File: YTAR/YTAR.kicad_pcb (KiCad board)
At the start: 2 copper layers, 37 parts, among them J1 STDC14, SW1 Tact, U1 STM32H750XBHx, Y1 25MHz

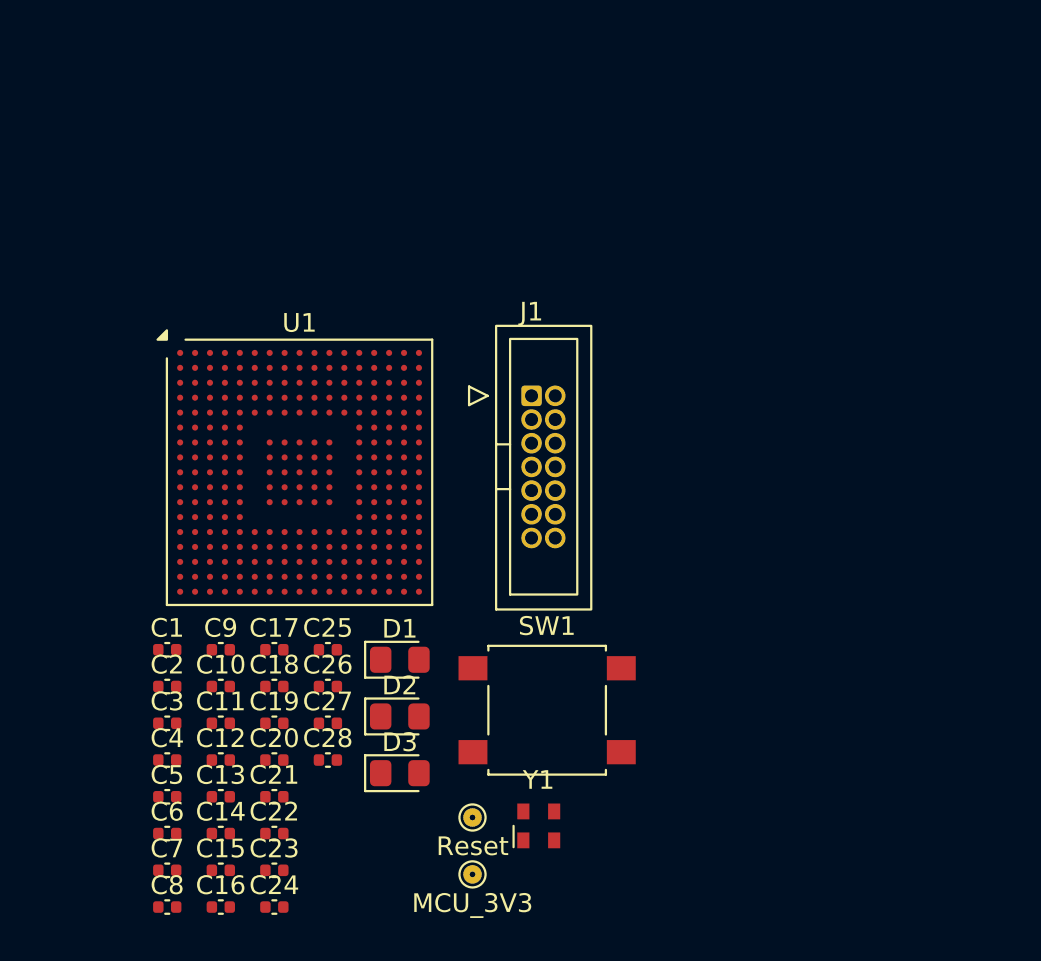
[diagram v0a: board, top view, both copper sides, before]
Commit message: DRAM added
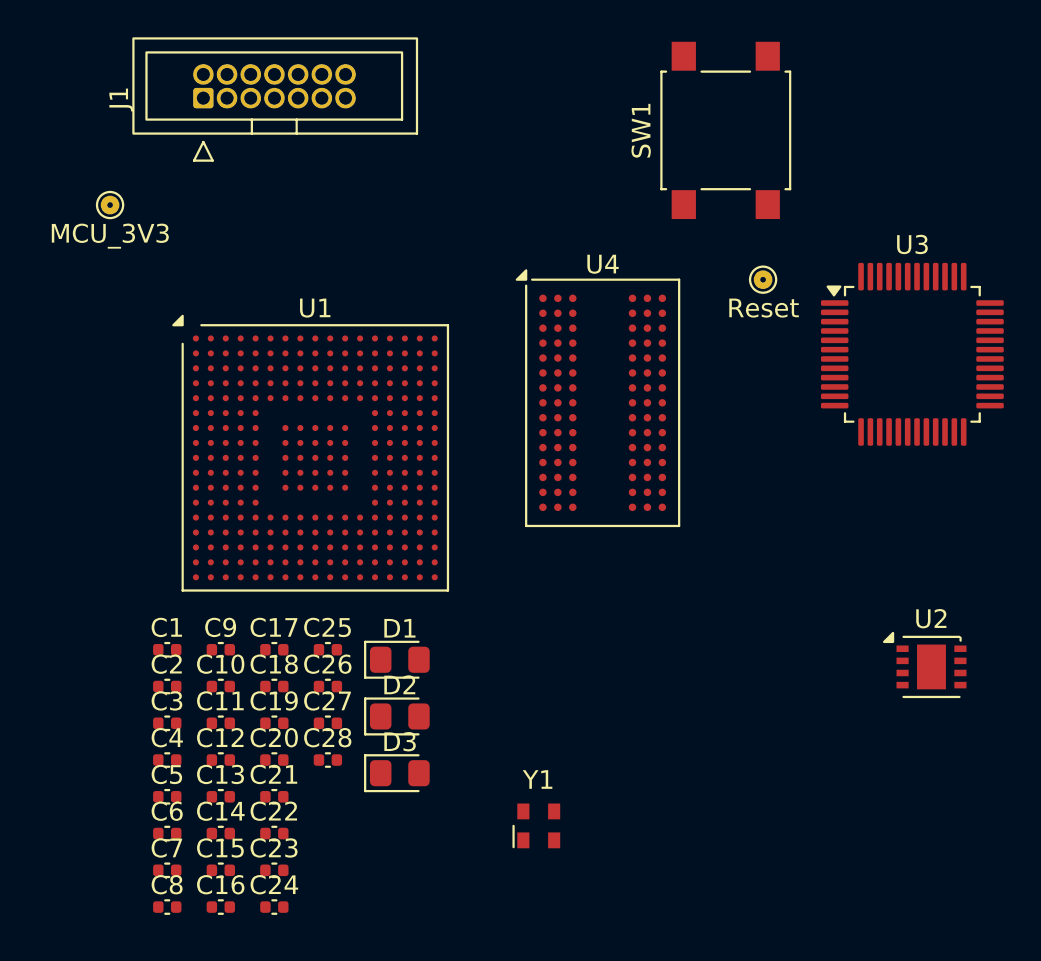
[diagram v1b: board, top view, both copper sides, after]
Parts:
- added U2: MCP2562-E-MF, Package_DFN_QFN:DFN-8-1EP_3x3mm_P0.65mm_EP1.55x2.4mm, F.Cu at (75.0, 48.8)
- added U3: DS90C124, Package_QFP:TQFP-48_7x7mm_P0.5mm, F.Cu at (74.0, 32.0)
- added U4: ~, Package_BGA:BGA-90_8.0x13.0mm_Layout2x3x15_P0.8mm, F.Cu at (57.4, 34.6)
- moved TP2 40.8 mm to (31.0, 24.0)
- moved TP1 32.8 mm to (66.0, 28.0)
- moved SW1 32.5 mm to (64.0, 20.0), turned to 90 degrees
- moved J1 23.7 mm to (36.0, 18.3), turned to 90 degrees
- moved U1 1.15 mm to (42.0, 37.5)

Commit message: Podłączono kwarc
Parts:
- added C29: 100n, Capacitor_SMD:C_0402_1005Metric, F.Cu at (35.1, 92.0)
- added C30: 100n, Capacitor_SMD:C_0402_1005Metric, F.Cu at (35.1, 94.0)
- added C31: 100n, Capacitor_SMD:C_0402_1005Metric, F.Cu at (35.1, 96.0)
- added C32: 100n, Capacitor_SMD:C_0402_1005Metric, F.Cu at (35.1, 98.0)
- added C33: 100n, Capacitor_SMD:C_0402_1005Metric, F.Cu at (35.1, 99.9)
- added C34: 100n, Capacitor_SMD:C_0402_1005Metric, F.Cu at (35.1, 101.9)
- added C35: 100n, Capacitor_SMD:C_0402_1005Metric, F.Cu at (35.1, 103.9)
- added C36: 100n, Capacitor_SMD:C_0402_1005Metric, F.Cu at (38.0, 92.0)
- added C37: 100n, Capacitor_SMD:C_0402_1005Metric, F.Cu at (38.0, 94.0)
- added C38: 100n, Capacitor_SMD:C_0402_1005Metric, F.Cu at (38.0, 96.0)
- added C39: 100n, Capacitor_SMD:C_0402_1005Metric, F.Cu at (38.0, 98.0)
- added C40: 100n, Capacitor_SMD:C_0402_1005Metric, F.Cu at (38.0, 99.9)
- added C41: 100n, Capacitor_SMD:C_0402_1005Metric, F.Cu at (38.0, 101.9)
- added C42: 100n, Capacitor_SMD:C_0402_1005Metric, F.Cu at (38.0, 103.9)
- added C43: 100n, Capacitor_SMD:C_0402_1005Metric, F.Cu at (40.8, 92.0)
- added C44: 100n, Capacitor_SMD:C_0402_1005Metric, F.Cu at (40.8, 94.0)
- added C45: 100n, Capacitor_SMD:C_0402_1005Metric, F.Cu at (40.8, 96.0)
- added C46: 100n, Capacitor_SMD:C_0402_1005Metric, F.Cu at (40.8, 98.0)
- added C47: 100n, Capacitor_SMD:C_0402_1005Metric, F.Cu at (40.8, 99.9)
- added C48: 100n, Capacitor_SMD:C_0402_1005Metric, F.Cu at (40.8, 101.9)
- added C49: 100n, Capacitor_SMD:C_0402_1005Metric, F.Cu at (40.8, 103.9)
- added C50: 100n, Capacitor_SMD:C_0402_1005Metric, F.Cu at (43.7, 92.0)
- added C51: 100n, Capacitor_SMD:C_0402_1005Metric, F.Cu at (43.7, 94.0)
- added C52: 100n, Capacitor_SMD:C_0402_1005Metric, F.Cu at (43.7, 96.0)
- added C53: 100n, Capacitor_SMD:C_0402_1005Metric, F.Cu at (43.7, 98.0)
- added J2: Conn_2x04_2.54mm_male_vertical, Connector_PinSocket_2.54mm:PinSocket_2x04_P2.54mm_Vertical, F.Cu at (50.0, 93.4)
- added J3: USB_C_Receptacle_USB2.0_NO_SBU, Connector_USB:USB_C_Receptacle_GCT_USB4085, F.Cu at (21.4, 29.0)
- added JP1: ~, MEMS_Passive:R_0805_2012Metric_Jumper_Open, F.Cu at (56.2, 74.6)
- added JP2: ~, MEMS_Passive:R_0805_2012Metric_Jumper_Open, F.Cu at (56.2, 77.6)
- added JP3: ~, MEMS_Passive:R_0805_2012Metric_Jumper_Open, F.Cu at (56.2, 80.5)
- added JP4: ~, MEMS_Passive:R_0805_2012Metric_Jumper_Open, F.Cu at (56.2, 83.5)
- added JP5: CAN, MEMS_Passive:R_0805_2012Metric_Jumper_Open, F.Cu at (56.2, 86.4)
- added JP6: DES_CLS_SEL, MEMS_Passive:R_0805_2012Metric_Jumper_Open, F.Cu at (56.2, 89.4)
- added R1: 10k, Resistor_SMD:R_0402_1005Metric, F.Cu at (35.1, 74.1)
- added R10: 10k, Resistor_SMD:R_0402_1005Metric, F.Cu at (38.0, 74.1)
- added R11: 10k, Resistor_SMD:R_0402_1005Metric, F.Cu at (38.0, 76.1)
- added R12: 10k, Resistor_SMD:R_0402_1005Metric, F.Cu at (38.0, 78.1)
- added R13: 10k, Resistor_SMD:R_0402_1005Metric, F.Cu at (38.0, 80.1)
- added R14: 10k, Resistor_SMD:R_0402_1005Metric, F.Cu at (38.0, 82.1)
- added R15: 10k, Resistor_SMD:R_0402_1005Metric, F.Cu at (38.0, 84.1)
- added R16: 10k, Resistor_SMD:R_0402_1005Metric, F.Cu at (38.0, 86.1)
- added R17: 10k, Resistor_SMD:R_0402_1005Metric, F.Cu at (38.0, 88.1)
- added R18: 10k, Resistor_SMD:R_0402_1005Metric, F.Cu at (38.0, 90.1)
- added R19: 10k, Resistor_SMD:R_0402_1005Metric, F.Cu at (40.9, 74.1)
- added R2: 10k, Resistor_SMD:R_0402_1005Metric, F.Cu at (35.1, 76.1)
- added R20: 120R, Resistor_SMD:R_0402_1005Metric, F.Cu at (40.9, 76.1)
- added R21: 620R, Resistor_SMD:R_0402_1005Metric, F.Cu at (40.9, 78.1)
- added R22: 49R9, Resistor_SMD:R_0402_1005Metric, F.Cu at (40.9, 80.1)
- added R23: 10k, Resistor_SMD:R_0402_1005Metric, F.Cu at (40.9, 82.1)
- added R24: 49R9, Resistor_SMD:R_0402_1005Metric, F.Cu at (40.9, 84.1)
- added R25: 33R, Resistor_SMD:R_0402_1005Metric, F.Cu at (40.9, 86.1)
- added R26: 33R, Resistor_SMD:R_0402_1005Metric, F.Cu at (40.9, 88.1)
- added R27: 33R, Resistor_SMD:R_0402_1005Metric, F.Cu at (40.9, 90.1)
- added R28: 33R, Resistor_SMD:R_0402_1005Metric, F.Cu at (43.8, 74.1)
- added R29: 33R, Resistor_SMD:R_0402_1005Metric, F.Cu at (43.8, 76.1)
- added R3: 10k, Resistor_SMD:R_0402_1005Metric, F.Cu at (35.1, 78.1)
- added R30: 33R, Resistor_SMD:R_0402_1005Metric, F.Cu at (43.8, 78.1)
- added R31: 33R, Resistor_SMD:R_0402_1005Metric, F.Cu at (43.8, 80.1)
- added R32: 33R, Resistor_SMD:R_0402_1005Metric, F.Cu at (43.8, 82.1)
- added R33: 33R, Resistor_SMD:R_0402_1005Metric, F.Cu at (43.8, 84.1)
- added R34: 33R, Resistor_SMD:R_0402_1005Metric, F.Cu at (43.8, 86.1)
- added R35: 33R, Resistor_SMD:R_0402_1005Metric, F.Cu at (43.8, 88.1)
- added R36: 33R, Resistor_SMD:R_0402_1005Metric, F.Cu at (43.8, 90.1)
- added R37: 33R, Resistor_SMD:R_0402_1005Metric, F.Cu at (46.8, 74.1)
- added R38: 33R, Resistor_SMD:R_0402_1005Metric, F.Cu at (46.8, 76.1)
- added R39: 33R, Resistor_SMD:R_0402_1005Metric, F.Cu at (46.8, 78.1)
- added R4: 10k, Resistor_SMD:R_0402_1005Metric, F.Cu at (35.1, 80.1)
- added R40: 33R, Resistor_SMD:R_0402_1005Metric, F.Cu at (46.8, 80.1)
- added R41: 33R, Resistor_SMD:R_0402_1005Metric, F.Cu at (46.8, 82.1)
- added R42: 33R, Resistor_SMD:R_0402_1005Metric, F.Cu at (46.8, 84.1)
- added R43: 33R, Resistor_SMD:R_0402_1005Metric, F.Cu at (46.8, 86.1)
- added R44: 33R, Resistor_SMD:R_0402_1005Metric, F.Cu at (46.8, 88.1)
- added R45: 33R, Resistor_SMD:R_0402_1005Metric, F.Cu at (46.8, 90.1)
- added R46: 33R, Resistor_SMD:R_0402_1005Metric, F.Cu at (49.7, 74.1)
- added R47: 33R, Resistor_SMD:R_0402_1005Metric, F.Cu at (49.7, 76.1)
- added R48: 33R, Resistor_SMD:R_0402_1005Metric, F.Cu at (49.7, 78.1)
- added R49: 33R, Resistor_SMD:R_0402_1005Metric, F.Cu at (49.7, 80.1)
- added R5: 10k, Resistor_SMD:R_0402_1005Metric, F.Cu at (35.1, 82.1)
- added R50: 33R, Resistor_SMD:R_0402_1005Metric, F.Cu at (49.7, 82.1)
- added R51: 33R, Resistor_SMD:R_0402_1005Metric, F.Cu at (49.7, 84.1)
- added R52: 33R, Resistor_SMD:R_0402_1005Metric, F.Cu at (49.7, 86.1)
- added R53: 33R, Resistor_SMD:R_0402_1005Metric, F.Cu at (49.7, 88.1)
- added R54: 33R, Resistor_SMD:R_0402_1005Metric, F.Cu at (49.7, 90.1)
- added R55: 33R, Resistor_SMD:R_0402_1005Metric, F.Cu at (52.6, 74.1)
- added R56: 33R, Resistor_SMD:R_0402_1005Metric, F.Cu at (52.6, 76.1)
- added R57: 33R, Resistor_SMD:R_0402_1005Metric, F.Cu at (52.6, 78.1)
- added R58: 33R, Resistor_SMD:R_0402_1005Metric, F.Cu at (52.6, 80.1)
- added R59: 33R, Resistor_SMD:R_0402_1005Metric, F.Cu at (52.6, 82.1)
- added R6: 10k, Resistor_SMD:R_0402_1005Metric, F.Cu at (35.1, 84.1)
- added R60: 33R, Resistor_SMD:R_0402_1005Metric, F.Cu at (52.6, 84.1)
- added R61: 33R, Resistor_SMD:R_0402_1005Metric, F.Cu at (52.6, 86.1)
- added R7: 10k, Resistor_SMD:R_0402_1005Metric, F.Cu at (35.1, 86.1)
- added R8: 10k, Resistor_SMD:R_0402_1005Metric, F.Cu at (35.1, 88.1)
- added R9: 10k, Resistor_SMD:R_0402_1005Metric, F.Cu at (35.1, 90.1)
- TP2: value MCU_3V3 -> 3V3
- moved TP2 72.3 mm to (53.8, 92.6)
- moved U4 27.6 mm to (70.4, 59.0)
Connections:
- C10 pad 1: VDDA -> +3.3V
- C11 pad 1: VDDA -> +3.3V
- C12 pad 1: VDDA -> +3.3V
- C13 pad 1: VDDA -> +3.3V
- C14 pad 1: VDDA -> +3.3V
- C15 pad 1: VDDA -> +3.3V
- C16 pad 1: VDDA -> +3.3V
- C17 pad 1: VDDA -> +3.3V
- C18 pad 1: VDDA -> +3.3V
- C19 pad 1: VDDA -> +3.3V
- C20 pad 1: VDDA -> +3.3V
- C21 pad 1: VDDA -> +3.3V
- C22 pad 1: VDDA -> +3.3V
- C23 pad 1: VDDA -> +3.3V
- C24 pad 1: VDDA -> +3.3V
- C26 pad 1: VDDA -> VDD_MCU
- C27 pad 1: VDDA -> VDD_MCU
- C3 pad 1: VDDA -> +3.3V
- C4 pad 1: VDDA -> +3.3V
- C5 pad 1: VDDA -> +3.3V
- C6 pad 1: VDDA -> +3.3V
- C7 pad 1: VDDA -> +3.3V
- C8 pad 1: VDDA -> +3.3V
- C9 pad 1: VDDA -> +3.3V
- J1 pad 3: VDDA -> VDD_MCU
- TP2 pad 1: VDDA -> +3.3V
- U1 pad B4: unconnected-(U1-PE1-PadB4) -> Net-(U1-PE1)
- U1 pad C1: unconnected-(U1-PC15-PadC1) -> Net-(U1-PC15)
- U1 pad C2: unconnected-(U1-PC14-PadC2) -> Net-(U1-PC14)
- U1 pad C4: unconnected-(U1-PE0-PadC4) -> Net-(U1-PE0)
- U1 pad D13: unconnected-(U1-PD0-PadD13) -> Net-(U1-PD0)
- U1 pad D6: unconnected-(U1-PG15-PadD6) -> Net-(U1-PG15)
- U1 pad E11: VDDA -> VDD_MCU
- U1 pad E12: unconnected-(U1-PD1-PadE12) -> Net-(U1-PD1)
- U1 pad E6: VDDA -> VDD_MCU
- U1 pad E9: VDDA -> VDD_MCU
- U1 pad F15: unconnected-(U1-PG8-PadF15) -> Net-(U1-PG8)
- U1 pad F5: VDDA -> VDD_MCU
- U1 pad G1: unconnected-(U1-PF2-PadG1) -> Net-(U1-PF2)
- U1 pad G13: VDDA -> VDD_MCU
- U1 pad G14: unconnected-(U1-PG5-PadG14) -> Net-(U1-PG5)
- U1 pad G3: unconnected-(U1-PF1-PadG3) -> Net-(U1-PF1)
- U1 pad G4: unconnected-(U1-PF0-PadG4) -> Net-(U1-PF0)
- U1 pad G5: VDDA -> VDD_MCU
- U1 pad H13: VDDA -> VDD_MCU
- U1 pad H14: unconnected-(U1-PG4-PadH14) -> Net-(U1-PG4)
- U1 pad H4: unconnected-(U1-PF3-PadH4) -> Net-(U1-PF3)
- U1 pad H5: VDDA -> VDD_MCU
- U1 pad J13: VDDA -> VDD_MCU
- U1 pad J4: unconnected-(U1-PF5-PadJ4) -> Net-(U1-PF5)
- U1 pad J5: unconnected-(U1-PF4-PadJ5) -> Net-(U1-PF4)
- U1 pad K13: VDDA -> VDD_MCU
- U1 pad K5: VDDA -> VDD_MCU
- U1 pad L1: VDDA -> VDD_MCU
- U1 pad L13: VDDA -> VDD_MCU
- U1 pad L5: VDDA -> VDD_MCU
- U1 pad M13: VDDA -> VDD_MCU
- U1 pad M5: VDDA -> VDD_MCU
- U1 pad N10: VDDA -> VDD_MCU
- U1 pad N11: VDDA -> VDD_MCU
- U1 pad N12: VDDA -> VDD_MCU
- U1 pad N7: VDDA -> VDD_MCU
- U1 pad N8: VDDA -> VDD_MCU
- U1 pad N9: unconnected-(U1-PE10-PadN9) -> Net-(U1-PE10)
- U1 pad P10: unconnected-(U1-PE11-PadP10) -> Net-(U1-PE11)
- U1 pad P17: VDDA -> VDD_MCU
- U1 pad P4: unconnected-(U1-PH5-PadP4) -> Net-(U1-PH5)
- U1 pad P7: unconnected-(U1-PF13-PadP7) -> Net-(U1-PF13)
- U1 pad P8: unconnected-(U1-PF14-PadP8) -> Net-(U1-PF14)
- U1 pad P9: unconnected-(U1-PE9-PadP9) -> Net-(U1-PE9)
- U1 pad R10: unconnected-(U1-PE12-PadR10) -> Net-(U1-PE12)
- U1 pad R11: unconnected-(U1-PE15-PadR11) -> /DQ12
- U1 pad R7: unconnected-(U1-PF12-PadR7) -> Net-(U1-PF12)
- U1 pad R9: unconnected-(U1-PF15-PadR9) -> Net-(U1-PF15)
- U1 pad T10: unconnected-(U1-PE13-PadT10) -> Net-(U1-PE13)
- U1 pad T11: unconnected-(U1-PH6-PadT11) -> Net-(U1-PH6)
- U1 pad T16: unconnected-(U1-PD10-PadT16) -> Net-(U1-PD10)
- U1 pad T17: unconnected-(U1-PD9-PadT17) -> Net-(U1-PD9)
- U1 pad T7: unconnected-(U1-PF11-PadT7) -> Net-(U1-PF11)
- U1 pad T8: unconnected-(U1-PG0-PadT8) -> Net-(U1-PG0)
- U1 pad T9: unconnected-(U1-PE8-PadT9) -> Net-(U1-PE8)
- U1 pad U10: unconnected-(U1-PE14-PadU10) -> Net-(U1-PE14)
- U1 pad U13: unconnected-(U1-PH7-PadU13) -> Net-(U1-PH7)
- U1 pad U16: unconnected-(U1-PD8-PadU16) -> Net-(U1-PD8)
- U1 pad U8: unconnected-(U1-PG1-PadU8) -> Net-(U1-PG1)
- U1 pad U9: unconnected-(U1-PE7-PadU9) -> Net-(U1-PE7)
- U2 pad 1: unconnected-(U2-TXD-Pad1) -> /CAN_TX
- U2 pad 2: unconnected-(U2-VSS-Pad2) -> GND
- U2 pad 3: unconnected-(U2-VDD-Pad3) -> VDD_CAN
- U2 pad 4: unconnected-(U2-RXD-Pad4) -> /CAN_RX
- U2 pad 5: unconnected-(U2-Vio-Pad5) -> VDD_CAN
- U2 pad 6: unconnected-(U2-CANL-Pad6) -> /CAN_L
- U2 pad 7: unconnected-(U2-CANH-Pad7) -> /CAN_H
- U2 pad 8: unconnected-(U2-SHDN-Pad8) -> Net-(U2-SHDN)
- U2 pad 9: unconnected-(U2-PAD-Pad9) -> GND
- U3 pad 1: unconnected-(U3-RPWDNB-Pad1) -> VDD_DES
- U3 pad 13: unconnected-(U3-ROUT15-Pad13) -> /ROUT15
- U3 pad 14: unconnected-(U3-ROUT14-Pad14) -> /ROUT14
- U3 pad 15: unconnected-(U3-ROUT13-Pad15) -> /ROUT13
- U3 pad 16: unconnected-(U3-ROUT12-Pad16) -> /ROUT12
- U3 pad 17: unconnected-(U3-LOCK-Pad17) -> /DES_LOCK
- U3 pad 18: unconnected-(U3-RCLK-Pad18) -> /DES_RCLK
- U3 pad 19: unconnected-(U3-VSSOR2-Pad19) -> GND
- U3 pad 2: unconnected-(U3-RESRVD-Pad2) -> GND
- U3 pad 20: unconnected-(U3-VDDOR2-Pad20) -> VDD_DES
- U3 pad 21: unconnected-(U3-ROUT11-Pad21) -> /ROUT11
- U3 pad 22: unconnected-(U3-ROUT10-Pad22) -> /ROUT10
- U3 pad 23: unconnected-(U3-ROUT9-Pad23) -> /ROUT9
- U3 pad 24: unconnected-(U3-ROUT8-Pad24) -> /ROUT8
- U3 pad 25: unconnected-(U3-ROUT7-Pad25) -> /ROUT7
- U3 pad 26: unconnected-(U3-ROUT6-Pad26) -> /ROUT6
- U3 pad 27: unconnected-(U3-ROUT5-Pad27) -> /ROUT5
- U3 pad 28: unconnected-(U3-ROUT4-Pad28) -> /ROUT4
- U3 pad 29: unconnected-(U3-VSSOR1-Pad29) -> GND
- U3 pad 30: unconnected-(U3-VDDOR1-Pad30) -> VDD_DES
- U3 pad 31: unconnected-(U3-ROUT3-Pad31) -> /ROUT3
- U3 pad 32: unconnected-(U3-ROUT2-Pad32) -> /ROUT2
- U3 pad 33: unconnected-(U3-ROUT1-Pad33) -> /ROUT1
- U3 pad 34: unconnected-(U3-ROUT0-Pad34) -> /ROUT0
- U3 pad 35: unconnected-(U3-VSSR0-Pad35) -> GND
- U3 pad 36: unconnected-(U3-VDDR0-Pad36) -> VDD_DES
- U3 pad 37: unconnected-(U3-VDDR1-Pad37) -> VDD_DES
- U3 pad 38: unconnected-(U3-VSSR1-Pad38) -> GND
- U3 pad 39: unconnected-(U3-VDDIR-Pad39) -> VDD_DES
- U3 pad 40: unconnected-(U3-VSSIR-Pad40) -> GND
- U3 pad 41: unconnected-(U3-RIN+-Pad41) -> Net-(U3-RIN+)
- U3 pad 42: unconnected-(U3-RIN--Pad42) -> Net-(U3-RIN-)
- U3 pad 43: unconnected-(U3-RRFB-Pad43) -> /DES_RRFB
- U3 pad 44: unconnected-(U3-VSSPR1-Pad44) -> GND
- U3 pad 45: unconnected-(U3-VDDPR1-Pad45) -> VDD_DES
- U3 pad 46: unconnected-(U3-VSSPR0-Pad46) -> GND
- U3 pad 47: unconnected-(U3-VDDPR0-Pad47) -> VDD_DES
- U3 pad 48: unconnected-(U3-REN-Pad48) -> VDD_DES
- U3 pad 7: unconnected-(U3-VDDOR3-Pad7) -> GND
- U3 pad 8: unconnected-(U3-VSSOR3-Pad8) -> VDD_DES
- U4 pad A1: unconnected-(U4-DQ26-PadA1) -> Net-(U4-DQ26)
- U4 pad A2: unconnected-(U4-DQ24-PadA2) -> Net-(U4-DQ24)
- U4 pad A3: unconnected-(U4-VSS-PadA3) -> GND
- U4 pad A7: unconnected-(U4-VDD-PadA7) -> VDD_DRAM
- U4 pad A8: unconnected-(U4-DQ23-PadA8) -> Net-(U4-DQ23)
- U4 pad A9: unconnected-(U4-DQ21-PadA9) -> Net-(U4-DQ21)
- U4 pad B1: unconnected-(U4-DQ28-PadB1) -> Net-(U4-DQ28)
- U4 pad B2: unconnected-(U4-VDDQ-PadB2) -> VDD_DRAM
- U4 pad B3: unconnected-(U4-VSSQ-PadB3) -> GND
- U4 pad B7: unconnected-(U4-VDDQ-PadB7) -> VDD_DRAM
- U4 pad B8: unconnected-(U4-VSSQ-PadB8) -> GND
- U4 pad B9: unconnected-(U4-DQ19-PadB9) -> Net-(U4-DQ19)
- U4 pad C1: unconnected-(U4-VSSQ-PadC1) -> GND
- U4 pad C2: unconnected-(U4-DQ27-PadC2) -> Net-(U4-DQ27)
- U4 pad C3: unconnected-(U4-DQ25-PadC3) -> Net-(U4-DQ25)
- U4 pad C7: unconnected-(U4-DQ22-PadC7) -> Net-(U4-DQ22)
- U4 pad C8: unconnected-(U4-DQ20-PadC8) -> Net-(U4-DQ20)
- U4 pad C9: unconnected-(U4-VDDQ-PadC9) -> VDD_DRAM
- U4 pad D1: unconnected-(U4-VSSQ-PadD1) -> GND
- U4 pad D2: unconnected-(U4-DQ29-PadD2) -> Net-(U4-DQ29)
- U4 pad D3: unconnected-(U4-DQ30-PadD3) -> Net-(U4-DQ30)
- U4 pad D7: unconnected-(U4-DQ17-PadD7) -> Net-(U4-DQ17)
- U4 pad D8: unconnected-(U4-DQ18-PadD8) -> Net-(U4-DQ18)
- U4 pad D9: unconnected-(U4-VDDQ-PadD9) -> VDD_DRAM
- U4 pad E1: unconnected-(U4-VDDQ-PadE1) -> VDD_DRAM
- U4 pad E2: unconnected-(U4-DQ31-PadE2) -> Net-(U4-DQ31)
- U4 pad E8: unconnected-(U4-DQ16-PadE8) -> Net-(U4-DQ16)
- U4 pad E9: unconnected-(U4-VSSQ-PadE9) -> GND
- U4 pad F1: unconnected-(U4-VSS-PadF1) -> GND
- U4 pad F2: unconnected-(U4-DQM3-PadF2) -> Net-(U4-DQM3)
- U4 pad F3: unconnected-(U4-A3-PadF3) -> /A3
- U4 pad F7: unconnected-(U4-A2-PadF7) -> /A2
- U4 pad F8: unconnected-(U4-DQM2-PadF8) -> Net-(U4-DQM2)
- U4 pad F9: unconnected-(U4-VDD-PadF9) -> VDD_DRAM
- U4 pad G1: unconnected-(U4-A4-PadG1) -> /A4
- U4 pad G2: unconnected-(U4-A5-PadG2) -> /A5
- U4 pad G3: unconnected-(U4-A6-PadG3) -> /A6
- U4 pad G7: unconnected-(U4-A10-PadG7) -> /A10
- U4 pad G8: unconnected-(U4-A0-PadG8) -> /A0
- U4 pad G9: unconnected-(U4-A1-PadG9) -> /A1
- U4 pad H1: unconnected-(U4-A7-PadH1) -> /A7
- U4 pad H2: unconnected-(U4-A8-PadH2) -> /A8
- U4 pad H8: unconnected-(U4-BA1-PadH8) -> /BA1
- U4 pad H9: unconnected-(U4-A11-PadH9) -> /A11
- U4 pad J1: unconnected-(U4-CLK-PadJ1) -> /SDN_CLK
- U4 pad J2: unconnected-(U4-CKE-PadJ2) -> /SDN_CKE
- U4 pad J3: unconnected-(U4-A9-PadJ3) -> /A9
- U4 pad J7: unconnected-(U4-BA0-PadJ7) -> /BA0
- U4 pad J8: unconnected-(U4-~{CS}-PadJ8) -> /SDN_NE
- U4 pad J9: unconnected-(U4-~{RAS}-PadJ9) -> /SDN_RAS
- U4 pad K1: unconnected-(U4-DQM1-PadK1) -> /NBL1
- U4 pad K7: unconnected-(U4-~{CAS}-PadK7) -> /SDN_CAS
- U4 pad K8: unconnected-(U4-~{WE}-PadK8) -> /SDN_WE
- U4 pad K9: unconnected-(U4-DQM0-PadK9) -> /NBL0
- U4 pad L1: unconnected-(U4-VDDQ-PadL1) -> VDD_DRAM
- U4 pad L2: unconnected-(U4-DQ8-PadL2) -> /DQ8
- U4 pad L3: unconnected-(U4-VSS-PadL3) -> GND
- U4 pad L7: unconnected-(U4-VDD-PadL7) -> VDD_DRAM
- U4 pad L8: unconnected-(U4-DQ7-PadL8) -> /DQ7
- U4 pad L9: unconnected-(U4-VSSQ-PadL9) -> GND
- U4 pad M1: unconnected-(U4-VSSQ-PadM1) -> GND
- U4 pad M2: unconnected-(U4-DQ10-PadM2) -> /DQ10
- U4 pad M3: unconnected-(U4-DQ9-PadM3) -> /DQ9
- U4 pad M7: unconnected-(U4-DQ6-PadM7) -> /DQ6
- U4 pad M8: unconnected-(U4-DQ5-PadM8) -> /DQ5
- U4 pad M9: unconnected-(U4-VDDQ-PadM9) -> VDD_DRAM
- U4 pad N1: unconnected-(U4-VSSQ-PadN1) -> GND
- U4 pad N2: unconnected-(U4-DQ12-PadN2) -> /DQ12
- U4 pad N3: unconnected-(U4-DQ14-PadN3) -> /DQ14
- U4 pad N7: unconnected-(U4-DQ1-PadN7) -> /DQ1
- U4 pad N8: unconnected-(U4-DQ3-PadN8) -> /DQ3
- U4 pad N9: unconnected-(U4-VDDQ-PadN9) -> VDD_DRAM
- U4 pad P1: unconnected-(U4-DQ11-PadP1) -> /DQ11
- U4 pad P2: unconnected-(U4-VDDQ-PadP2) -> VDD_DRAM
- U4 pad P3: unconnected-(U4-VSSQ-PadP3) -> GND
- U4 pad P7: unconnected-(U4-VDDQ-PadP7) -> VDD_DRAM
- U4 pad P8: unconnected-(U4-VSSQ-PadP8) -> GND
- U4 pad P9: unconnected-(U4-DQ4-PadP9) -> /DQ4
- U4 pad R1: unconnected-(U4-DQ13-PadR1) -> /DQ13
- U4 pad R2: unconnected-(U4-DQ15-PadR2) -> /DQ15
- U4 pad R3: unconnected-(U4-VSS-PadR3) -> GND
- U4 pad R7: unconnected-(U4-VDD-PadR7) -> VDD_DRAM
- U4 pad R8: unconnected-(U4-DQ0-PadR8) -> /DQ0
- U4 pad R9: unconnected-(U4-DQ2-PadR9) -> /DQ2
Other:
- copper layers 2 -> 6

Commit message: Basic layout
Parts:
- added C54: 2.2u, Capacitor_SMD:C_0402_1005Metric, F.Cu at (39.5, 48.0)
- added C55: 4.7n, Capacitor_SMD:C_0402_1005Metric, F.Cu at (25.5, 39.0)
- added C56: 8.2p, Capacitor_SMD:C_0402_1005Metric, F.Cu at (18.0, 37.9)
- added C57: 8.2p, Capacitor_SMD:C_0402_1005Metric, F.Cu at (20.0, 37.9)
- added J5: USB_C_USB4085-GF-A, Connector_USB:USB_C_Receptacle_GCT_USB4085, F.Cu at (18.4, 21.6)
- added J6: IO, Connector_Hirose:Hirose_DF52-8S-0.8H_1x08-1MP_P0.80mm_Horizontal, F.Cu at (14.0, 36.0)
- added JP7: BOOT, MEMS_Passive:R_0805_2012Metric_Jumper_Open, F.Cu at (1.91, 31.0)
- added R62: 620R, Resistor_SMD:R_0402_1005Metric, F.Cu at (30.0, 17.0)
- added R63: 620R, Resistor_SMD:R_0402_1005Metric, F.Cu at (32.0, 17.0)
- added R64: 10k, Resistor_SMD:R_0402_1005Metric, F.Cu at (26.0, 19.0)
- added R65: 10k, Resistor_SMD:R_0402_1005Metric, F.Cu at (28.0, 19.0)
- added R66: 0R, Resistor_SMD:R_0402_1005Metric, F.Cu at (18.0, 32.0)
- added R67: 5k1, Resistor_SMD:R_0402_1005Metric, B.Cu at (14.5, 24.0)
- added R68: 5k1, Resistor_SMD:R_0402_1005Metric, B.Cu at (14.5, 26.0)
- C29, C30, C31, C32, C33, C34, C35, C36, C37, C38, C39, C40, C41, C42: moved to B.Cu
- J2: value Conn_2x04_2.54mm_male_vertical -> CAMERA; footprint Connector_PinSocket_2.54mm:PinSocket_2x04_P2.54mm_Vertical -> Connector_Hirose:Hirose_DF52-8S-0.8H_1x08-1MP_P0.80mm_Horizontal
- J3: value USB_C_Receptacle_USB2.0_NO_SBU -> Micro_Sd; footprint Connector_USB:USB_C_Receptacle_GCT_USB4085 -> Connector_Card:microSD_HC_Hirose_DM3AT-SF-PEJM5; moved to B.Cu
- JP6: value DES_CLS_SEL -> DES_CLK_SEL
- SW1: footprint Button_Switch_SMD:SW_SPST_B3S-1000 -> Button_Switch_SMD:SW_SPST_B3U-1000P
- moved TP2 82.4 mm to (4.00, 27.0)
- moved R9 76.4 mm to (60.5, 18.0)
- moved R8 72.9 mm to (58.5, 19.0), turned to 180 degrees
- moved C29 71.4 mm to (53.9, 23.1), turned to 180 degrees
- moved C30 71.4 mm to (53.9, 25.1), turned to 180 degrees
- moved C31 71.4 mm to (53.9, 27.1), turned to 180 degrees
- moved C32 71.4 mm to (53.9, 29.0), turned to 180 degrees
- moved C33 71.4 mm to (53.9, 31.0), turned to 180 degrees
- moved C34 71.4 mm to (53.9, 33.0), turned to 180 degrees
- moved C35 71.4 mm to (53.9, 34.9), turned to 180 degrees
- moved R18 71.3 mm to (51.0, 20.0)
- moved R17 70.4 mm to (51.5, 19.0)
- moved C36 70.1 mm to (51.0, 23.1), turned to 180 degrees
- moved C37 70.1 mm to (51.0, 25.1), turned to 180 degrees
- moved C38 70.1 mm to (51.0, 27.1), turned to 180 degrees
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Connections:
- C25 pad 1: Net-(C25-Pad1) -> VDDA
- C26 pad 1: VDD_MCU -> VDDA
- C27 pad 1: VDD_MCU -> VDDA
- D1 pad 1: unconnected-(D1-K-Pad1) -> Net-(D1-K)
- D1 pad 2: unconnected-(D1-A-Pad2) -> +3.3V
- D2 pad 1: unconnected-(D2-K-Pad1) -> Net-(D2-K)
- D2 pad 2: unconnected-(D2-A-Pad2) -> +3.3V
- D3 pad 1: unconnected-(D3-K-Pad1) -> Net-(D3-K)
- D3 pad 2: unconnected-(D3-A-Pad2) -> +3.3V
- J1 pad 3: VDD_MCU -> VDDA
- J2 pad 1: /CAM_LVDS_L -> +12V_CAM
- J2 pad 2: /CAM_LVDS_H -> GND
- J2 pad 3: unconnected-(J2-Pin_3-Pad3) -> /CAM_LVDS_H
- J2 pad 4: unconnected-(J2-Pin_4-Pad4) -> /CAM_LVDS_L
- J2 pad 5: /CAM_VCC -> /CAM_CAN_H
- J2 pad 6: /CAM_GND -> /CAM_CAN_L
- J2 pad 7: /CAM_CAN_L -> unconnected-(J2-Pin_7-Pad7)
- J2 pad 8: /CAM_CAN_H -> unconnected-(J2-Pin_8-Pad8)
- JP1 pad 2: VDD_MCU -> VDDA
- R21 pad 1: unconnected-(R21-Pad1) -> Net-(D3-K)
- R21 pad 2: unconnected-(R21-Pad2) -> GND
- U1 pad A6: Net-(C25-Pad1) -> VDDA
- U1 pad B1: unconnected-(U1-VBAT-PadB1) -> VDDA
- U1 pad C17: Net-(C25-Pad1) -> VDDA
- U1 pad E11: VDD_MCU -> VDDA
- U1 pad E16: unconnected-(U1-PA12-PadE16) -> /D+
- U1 pad E17: unconnected-(U1-PA11-PadE17) -> /D-
- U1 pad E6: VDD_MCU -> VDDA
- U1 pad E7: unconnected-(U1-PDR_ON-PadE7) -> Net-(U1-PDR_ON)
- U1 pad E8: unconnected-(U1-BOOT0-PadE8) -> /BOOT0
- U1 pad E9: VDD_MCU -> VDDA
- U1 pad F17: /VDD_33_USB -> VDDA
- U1 pad F5: VDD_MCU -> VDDA
- U1 pad G13: VDD_MCU -> VDDA
- U1 pad G17: /VDD_50_USB -> VDDA
- U1 pad G5: VDD_MCU -> VDDA
- U1 pad H13: VDD_MCU -> VDDA
- U1 pad H5: VDD_MCU -> VDDA
- U1 pad J13: VDD_MCU -> VDDA
- U1 pad K13: VDD_MCU -> VDDA
- U1 pad K5: VDD_MCU -> VDDA
- U1 pad L1: VDD_MCU -> VDDA
- U1 pad L13: VDD_MCU -> VDDA
- U1 pad L5: VDD_MCU -> VDDA
- U1 pad M1: unconnected-(U1-VREF+-PadM1) -> VDDA
- U1 pad M13: VDD_MCU -> VDDA
- U1 pad M5: VDD_MCU -> VDDA
- U1 pad N1: unconnected-(U1-VREF--PadN1) -> GND
- U1 pad N10: VDD_MCU -> VDDA
- U1 pad N11: VDD_MCU -> VDDA
- U1 pad N12: VDD_MCU -> VDDA
- U1 pad N7: VDD_MCU -> VDDA
- U1 pad N8: VDD_MCU -> VDDA
- U1 pad P17: VDD_MCU -> VDDA
- U1 pad U12: Net-(C25-Pad1) -> VDDA
- Y1 pad 1: unconnected-(Y1-Pad1) -> Net-(C56-Pad1)
- Y1 pad 2: unconnected-(Y1-Pad2) -> GND
- Y1 pad 3: unconnected-(Y1-Pad3) -> /RCC_OUT
- Y1 pad 4: unconnected-(Y1-Pad4) -> GND
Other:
- board outline added: 50 x 50 mm
